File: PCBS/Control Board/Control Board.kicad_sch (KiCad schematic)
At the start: 24 parts, among them J1 S3B-PH-K-S(LF)(SN), J2 Conn_02x03_Odd_Even, J3 S2B-PH-K-S(LF)(SN), U1 ATmega328-MM, U2 RP400N501A-TR-FE, U3 LDL1117, U4 TXU0304, U5 HP203B, Y1 Resonator

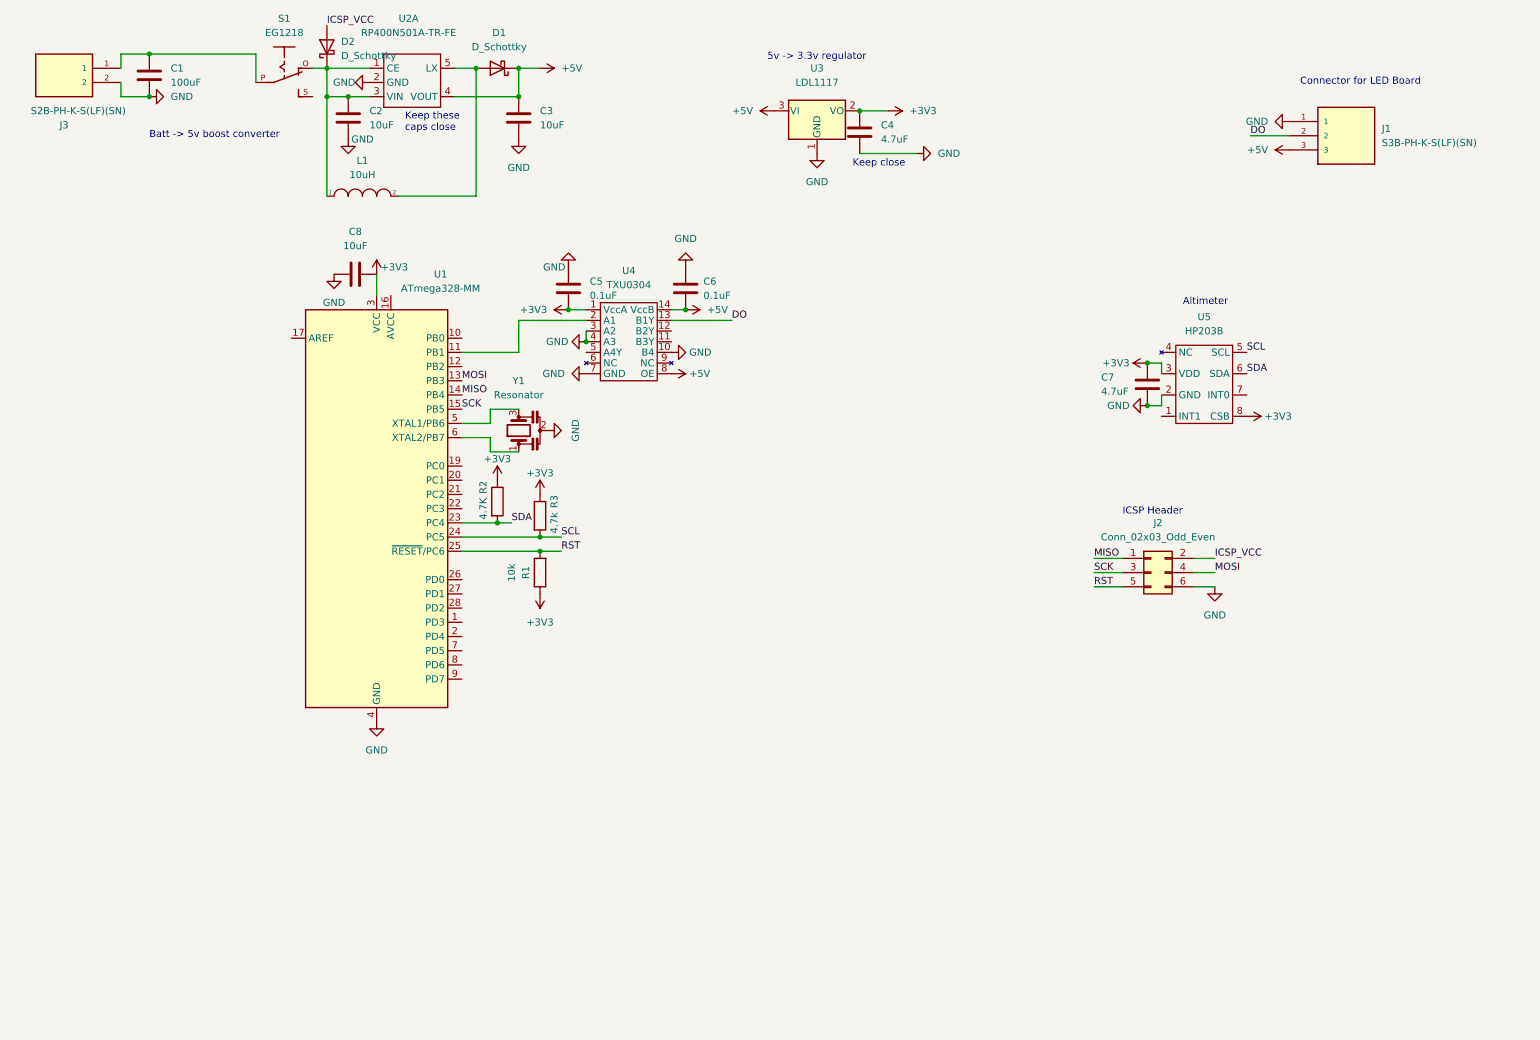
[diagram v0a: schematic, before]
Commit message: Updated schematic, started updating layout
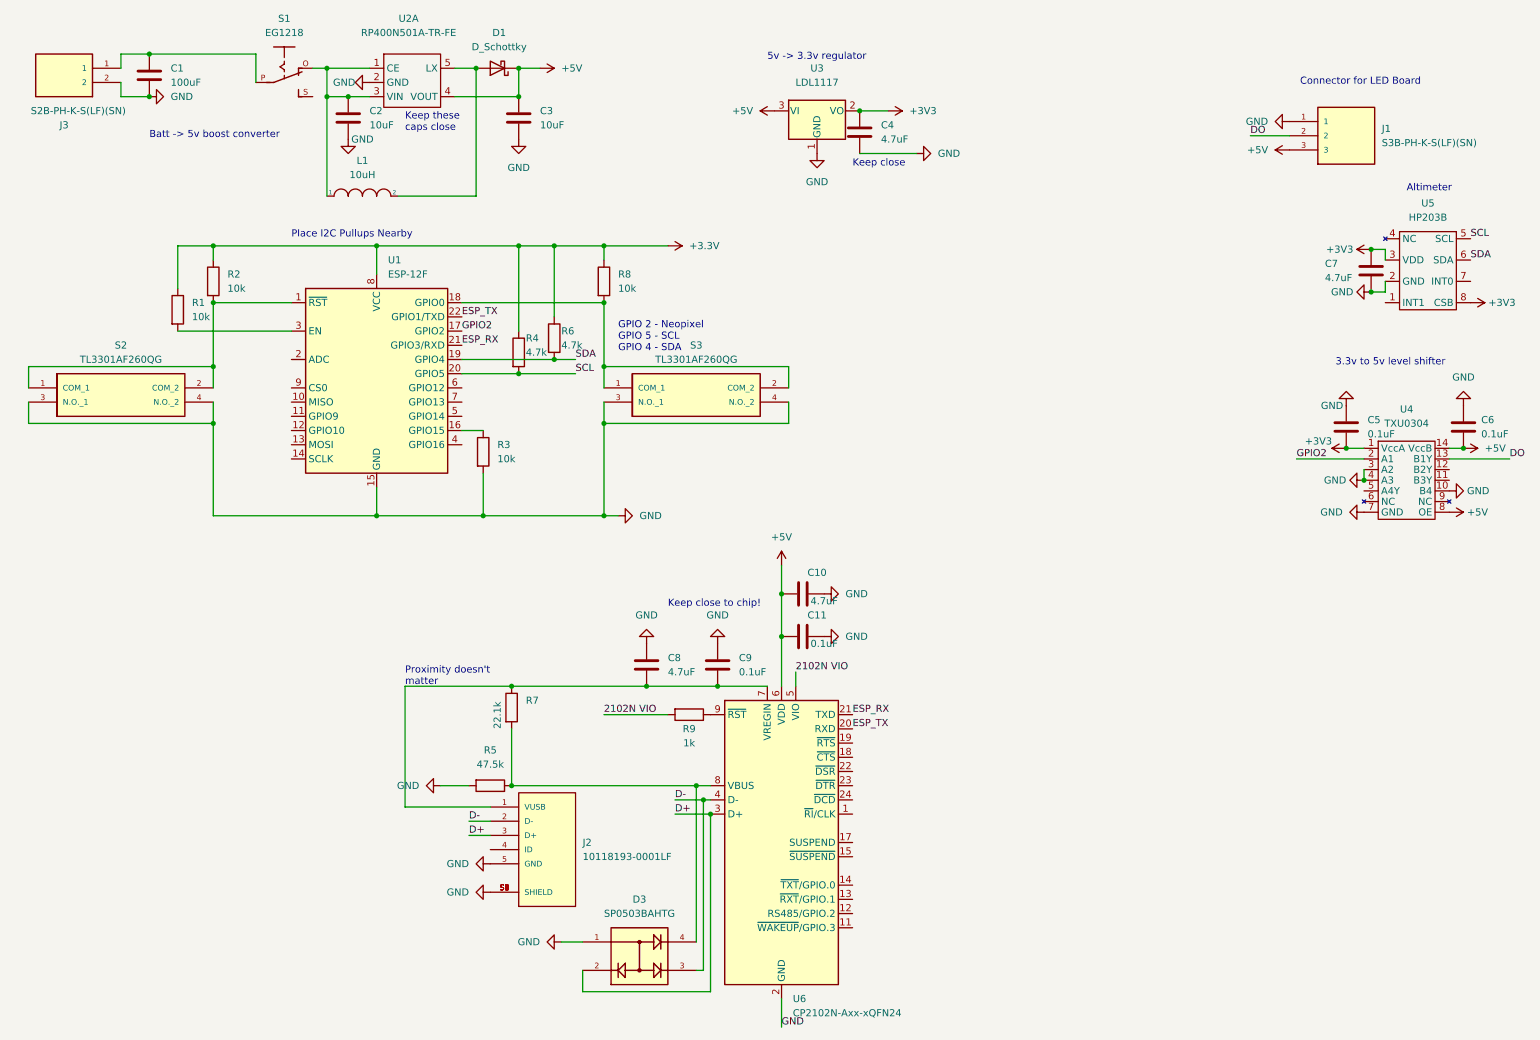
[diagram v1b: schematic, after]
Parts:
- removed D2: D_Schottky, Diode_SMD:D_SOD-123, symbol Device:D_Schottky
- removed J2: Conn_02x03_Odd_Even, Connector_PinHeader_2.54mm:PinHeader_2x03_P2.54mm_Vertical, symbol Connector_Generic:Conn_02x03_Odd_Even
- removed U1: ATmega328-MM, Package_DFN_QFN:QFN-28-1EP_4x4mm_P0.45mm_EP2.4x2.4mm, symbol MCU_Microchip_ATmega:ATmega328-MM
- removed Y1: Resonator, CSTNE16M0V530000R0:OSC_CSTNE16M0V530000R0, symbol Device:Resonator
- added C10: 4.7uF, Capacitor_SMD:C_0402_1005Metric, symbol Device:C
- added C11, C9: 0.1uF, Capacitor_SMD:C_0402_1005Metric, symbol Device:C
- added D3: SP0503BAHTG, SP0503BAHTG:SOT143, symbol SP0503BAHTG:SP0503BAHTG
- added J2: 10118193-0001LF, 10118193-0001LF Micro B Port:FCI_10118193-0001LF, symbol 10118193-0001LF:10118193-0001LF
- added R4, R6: 4.7k, Resistor_SMD:R_0402_1005Metric, symbol Device:R
- added R5: 47.5k, Resistor_SMD:R_0402_1005Metric, symbol Device:R
- added R7: 22.1k, Resistor_SMD:R_0402_1005Metric, symbol Device:R
- added R8: 10k, Resistor_SMD:R_0402_1005Metric, symbol Device:R
- added R9: 1k, Resistor_SMD:R_0603_1608Metric, symbol Device:R
- added S2, S3: TL3301AF260QG, TL3301AF260QG Pushbutton:TL3301AF260QG, symbol TL3301AF260QG:TL3301AF260QG
- added U1: ESP-12F, RF_Module:ESP-12E, symbol RF_Module:ESP-12F
- added U6: CP2102N-Axx-xQFN24, Package_DFN_QFN:QFN-24-1EP_4x4mm_P0.5mm_EP2.6x2.6mm, symbol Interface_USB:CP2102N-Axx-xQFN24
- C8: value 10uF -> 4.7uF; footprint Capacitor_SMD:C_0805_2012Metric -> Capacitor_SMD:C_0402_1005Metric; LCSC (none) -> C129235
- R1: footprint Resistor_SMD:R_0201_0603Metric -> Resistor_SMD:R_0402_1005Metric; LCSC (none) -> C17414
- R2: value 4.7K -> 10k; LCSC (none) -> C17414
- R3: value 4.7k -> 10k; LCSC (none) -> C17414
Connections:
- net +3V3: now also R4.1, R6.1, R8.1, U1.8 (VCC); no longer C8.1, R3.1
- net +5V: now also C10.2, C11.2, U6.6 (VDD)
- net GND: now also C8.1, R3.2, C10.1, C11.1, C9.1, D3.1, J2.5 (GND), J2.S1 (SHIELD), J2.S2 (SHIELD), J2.S3 (SHIELD), J2.S4 (SHIELD), J2.S5 (SHIELD), J2.S6 (SHIELD), R5.2, S2.3 (N.O._1), S2.4 (N.O._2), S3.3 (N.O._1), S3.4 (N.O._2), U1.15 (GND), U6.2 (GND), U6.25 (GND); no longer C8.2
- net SCL: now also R4.2, U1.20 (GPIO5); no longer R3.2
- net SDA: now also R6.2, U1.19 (GPIO4); no longer R2.2
- net GPIO2: now reaches U4.2 (A1)
- net GPIO2: now also U1.17 (GPIO2)
- net RST: no longer names the net of R1.2
- net RST: now also U1.3 (EN)
- new net: C8.2, C9.2, J2.1 (VUSB), R7.1, U6.7 (VREGIN)
- new net: D3.4, R5.1, R7.2, U6.8 (VBUS)
- new net: R9.1, U6.9 (~{RST})
- new net: R2.2, S2.1 (COM_1), S2.2 (COM_2), U1.1 (~{RST})
- new net: R3.1, U1.16 (GPIO15)
- new net: R8.2, S3.1 (COM_1), S3.2 (COM_2), U1.18 (GPIO0)
- new net 2102N VIO: R9.2, U6.5 (VIO)
- new net D+: D3.2, J2.3 (D+), U6.3 (D+)
- new net D-: D3.3, J2.2 (D-), U6.4 (D-)
- new net ESP_RX: U1.21 (GPIO3/RXD), U6.21 (TXD)
- new net ESP_TX: U1.22 (GPIO1/TXD), U6.20 (RXD)
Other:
- note added: "3.3v to 5v level shifter"
- note added: "GPIO 2 - Neopixel GPIO 5 - SCL GPIO 4 - SDA"
- note added: "Keep close to chip!"
- note added: "Place I2C Pullups Nearby"
- note added: "Proximity doesn't matter"
- note removed: "ICSP Header"
- moved on the sheet: C5, C6, C7, U4, U5
